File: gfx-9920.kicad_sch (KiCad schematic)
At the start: 0 parts

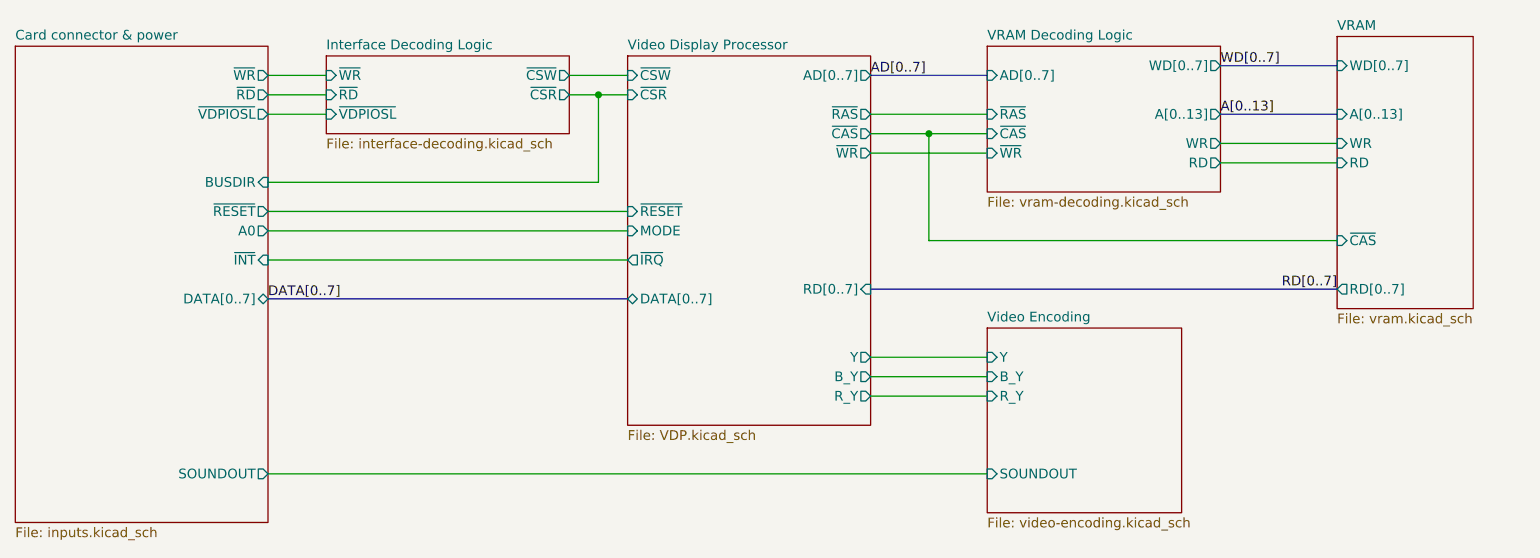
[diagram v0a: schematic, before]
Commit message: Update to latest Artemisa kicadlibs
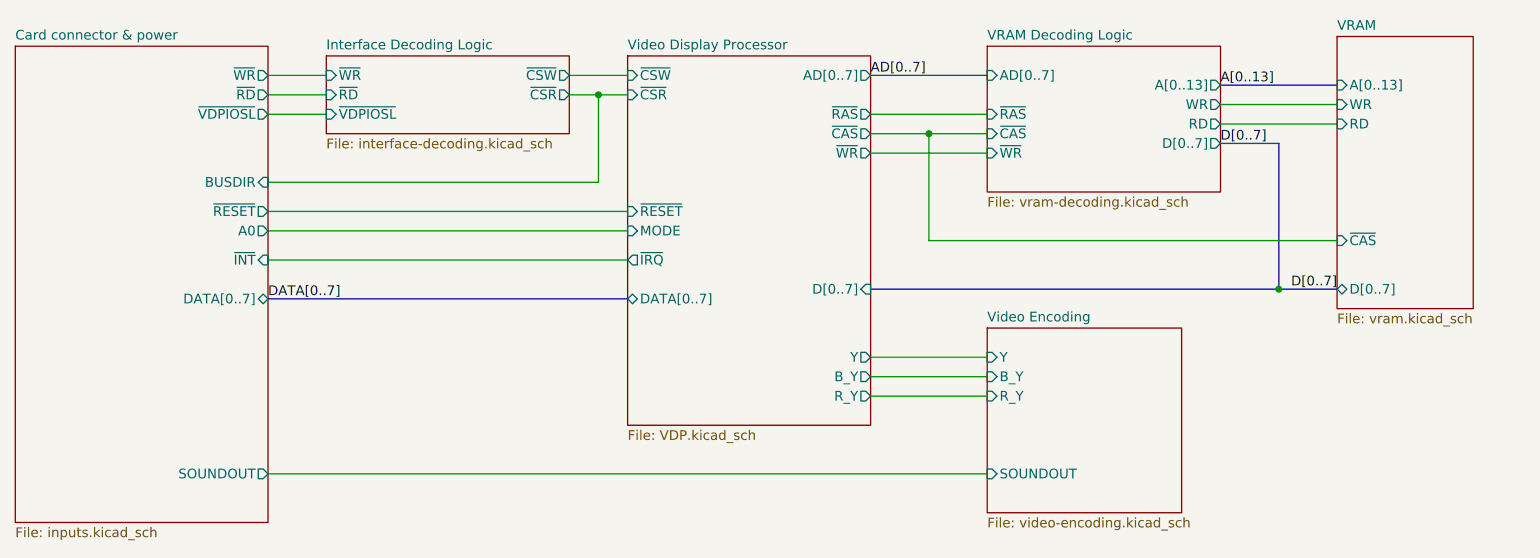
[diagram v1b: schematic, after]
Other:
- sheet VRAM ports: added D[0..7]; removed RD[0..7], WD[0..7]
- sheet VRAM Decoding Logic ports: added D[0..7]; removed WD[0..7]
- sheet Video Display Processor ports: added D[0..7]; removed RD[0..7]
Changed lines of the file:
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@@
+	)
+	(junction
+		(at 252.73 147.32)
+		(diameter 0)
+		(color 0 0 0 0)
 	)
 	(junction
@@
 	(bus
 		(pts
-			(xy 260.35 147.32) (xy 199.39 147.32)
+			(xy 252.73 128.27) (xy 252.73 147.32)
+		)
+		(stroke
+			(width 0)
+			(type default)
+		)
+	)
+	(bus
+		(pts
+			(xy 260.35 147.32) (xy 252.73 147.32)
 		)
 		(stroke
@@
 		)
 	)
+	(bus
+		(pts
+			(xy 252.73 147.32) (xy 199.39 147.32)
+		)
+		(stroke
+			(width 0)
+			(type default)
+		)
+	)
 	(wire
 		(pts
@@
 	(bus
 		(pts
-			(xy 245.11 118.11) (xy 260.35 118.11)
+			(xy 245.11 128.27) (xy 252.73 128.27)
 		)
 		(stroke
@@
 	(wire
 		(pts
-			(xy 245.11 128.27) (xy 260.35 128.27)
-		)
-		(stroke
-			(width 0)
-			(type default)
-		)
-	)
-	(wire
-		(pts
-			(xy 245.11 130.81) (xy 260.35 130.81)
+			(xy 245.11 123.19) (xy 260.35 123.19)
+		)
+		(stroke
+			(width 0)
+			(type default)
+		)
+	)
+	(wire
+		(pts
+			(xy 245.11 125.73) (xy 260.35 125.73)
 		)
 		(stroke
@@
 	(bus
 		(pts
-			(xy 260.35 124.46) (xy 245.11 124.46)
+			(xy 260.35 120.65) (xy 245.11 120.65)
 		)
 		(stroke
@@
 		)
 	)
-	(label "RD[0..7]"
+	(label "D[0..7]"
 		(at 260.35 147.32 180)
 		(effects
@@
 	)
 	(label "A[0..13]"
-		(at 245.11 124.46 0)
+		(at 245.11 120.65 0)
 		(effects
 			(font
@@
 		)
 	)
-	(label "WD[0..7]"
-		(at 245.11 118.11 0)
+	(label "D[0..7]"
+		(at 245.11 128.27 0)
 		(effects
 			(font
@@
 			)
 		)
-		(pin "RD[0..7]" input
+		(pin "D[0..7]" input
 			(at 199.39 147.32 0)
 			(effects
@@
 			)
 		)
-		(pin "WD[0..7]" output
-			(at 245.11 118.11 0)
+		(pin "D[0..7]" output
+			(at 245.11 128.27 0)
 			(effects
 				(font
@@
 		)
 		(pin "WR" output
-			(at 245.11 128.27 0)
+			(at 245.11 123.19 0)
 			(effects
 				(font
@@
 		)
 		(pin "RD" output
-			(at 245.11 130.81 0)
+			(at 245.11 125.73 0)
 			(effects
 				(font
@@
 		)
 		(pin "A[0..13]" output
-			(at 245.11 124.46 0)
+			(at 245.11 120.65 0)
 			(effects
 				(font
@@
 		)
 		(pin "A[0..13]" input
-			(at 260.35 124.46 180)
+			(at 260.35 120.65 180)
 			(effects
 				(font
@@
 		)
 		(pin "RD" input
-			(at 260.35 130.81 180)
+			(at 260.35 125.73 180)
 			(effects
 				(font
@@
 		)
 		(pin "WR" input
-			(at 260.35 128.27 180)
+			(at 260.35 123.19 180)
 			(effects
 				(font
@@
 			)
 		)
-		(pin "RD[0..7]" output
+		(pin "D[0..7]" bidirectional
 			(at 260.35 147.32 180)
 			(effects
 				(font
-					(size 1.27 1.27)
-				)
-				(justify left)
-			)
-		)
-		(pin "WD[0..7]" input
-			(at 260.35 118.11 180)
-			(effects
-				(font
